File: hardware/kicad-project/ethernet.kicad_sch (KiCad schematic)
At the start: 43 parts, among them IC7 IC_ETH_PHY_LAN8742A, J2 J_RJ45_SKT_MAG_LED, Y3 25MHZ

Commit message: Added MCU decoupling
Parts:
- renumbered C45 to C30, C46 to C31, C47 to C32, C48 to C33, C49 to C34, C50 to C35, C51 to C36, C52 to C37, C53 to C38, C54 to C39, IC7 to IC6, J2 to J8, NT1 to NT3, R50 to R20, R51 to R21, R52 to R22, R56 to R23, R59 to R24, R54 to R25, R57 to R26, R58 to R27, R53 to R28, R55 to R29, R60 to R30, R61 to R31, R62 to R32, R63 to R33, R64 to R34, R47 to R35, R48 to R36, R49 to R37, TP23 to TP19, TP24 to TP20, TP25 to TP21, TP26 to TP22, TP27 to TP23, TP28 to TP24, Y3 to Y2
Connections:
- net GNDA renamed Earth

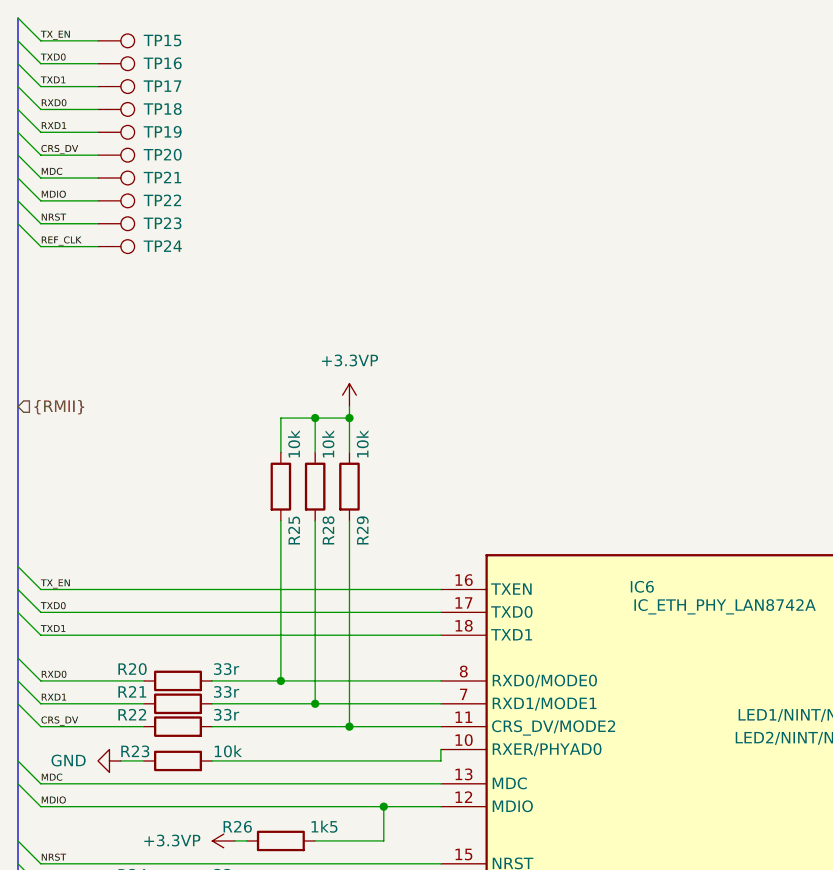
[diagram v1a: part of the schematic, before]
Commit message: Adding test points
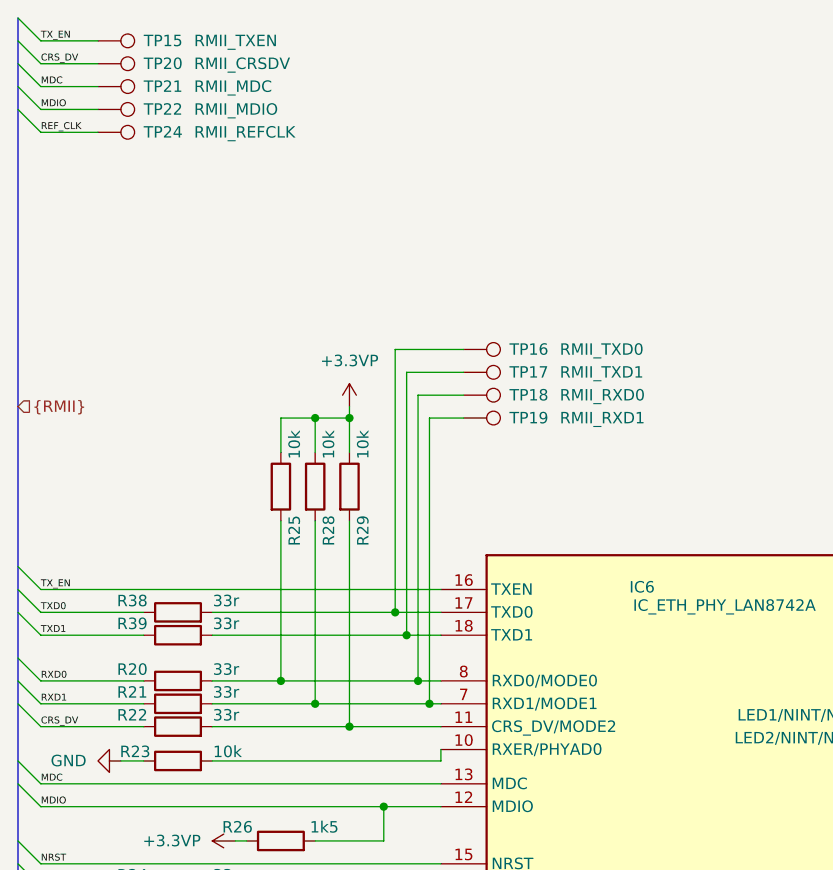
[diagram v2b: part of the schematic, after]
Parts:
- removed TP16, TP17, TP18, TP19, TP23: (no value), TestPoint:TestPoint_THTPad_D1.0mm_Drill0.5mm, symbol Connector:TestPoint
- added R38, R39: 33r, Resistor_SMD:R_0603_1608Metric_Pad0.98x0.95mm_HandSolder, symbol #InvenTree:R_33r_0603
- added TP16: RMII_TXD0, ebnx_footprints:TestPoint_THTPad_D1.0mm_Drill0.5mm_annotated, symbol ebnx_symbols:TestPoint_Annotated_Silkscreen
- added TP17: RMII_TXD1, ebnx_footprints:TestPoint_THTPad_D1.0mm_Drill0.5mm_annotated, symbol ebnx_symbols:TestPoint_Annotated_Silkscreen
- added TP18: RMII_RXD0, ebnx_footprints:TestPoint_THTPad_D1.0mm_Drill0.5mm_annotated, symbol ebnx_symbols:TestPoint_Annotated_Silkscreen
- added TP19: RMII_RXD1, ebnx_footprints:TestPoint_THTPad_D1.0mm_Drill0.5mm_annotated, symbol ebnx_symbols:TestPoint_Annotated_Silkscreen
- TP15: value (none) -> RMII_TXEN; footprint TestPoint:TestPoint_THTPad_D1.0mm_Drill0.5mm -> ebnx_footprints:TestPoint_THTPad_D1.0mm_Drill0.5mm_annotated; symbol Connector:TestPoint -> ebnx_symbols:TestPoint_Annotated_Silkscreen; now in the parts list
- TP20: value (none) -> RMII_CRSDV; footprint TestPoint:TestPoint_THTPad_D1.0mm_Drill0.5mm -> ebnx_footprints:TestPoint_THTPad_D1.0mm_Drill0.5mm_annotated; symbol Connector:TestPoint -> ebnx_symbols:TestPoint_Annotated_Silkscreen; now in the parts list
- TP21: value (none) -> RMII_MDC; footprint TestPoint:TestPoint_THTPad_D1.0mm_Drill0.5mm -> ebnx_footprints:TestPoint_THTPad_D1.0mm_Drill0.5mm_annotated; symbol Connector:TestPoint -> ebnx_symbols:TestPoint_Annotated_Silkscreen; now in the parts list
- TP22: value (none) -> RMII_MDIO; footprint TestPoint:TestPoint_THTPad_D1.0mm_Drill0.5mm -> ebnx_footprints:TestPoint_THTPad_D1.0mm_Drill0.5mm_annotated; symbol Connector:TestPoint -> ebnx_symbols:TestPoint_Annotated_Silkscreen; now in the parts list
- TP24: value (none) -> RMII_REFCLK; footprint TestPoint:TestPoint_THTPad_D1.0mm_Drill0.5mm -> ebnx_footprints:TestPoint_THTPad_D1.0mm_Drill0.5mm_annotated; symbol Connector:TestPoint -> ebnx_symbols:TestPoint_Annotated_Silkscreen; now in the parts list
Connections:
- net TXD0: now also R38.1; no longer IC6.17 (TXD0)
- net TXD1: now also R39.1; no longer IC6.18 (TXD1)
- net at IC6.8 (RXD0/MODE0), R20.2, R25.2: now also TP18.1
- net at IC6.7 (RXD1/MODE1), R21.2, R28.2: now also TP19.1
- new net: IC6.17 (TXD0), R38.2, TP16.1
- new net: IC6.18 (TXD1), R39.2, TP17.1
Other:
- moved on the sheet: TP20, TP21, TP22, TP24

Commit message: v0.5 routing complete
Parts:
- removed C38, C39: 100nF, Capacitor_SMD:C_0603_1608Metric_Pad1.08x0.95mm_HandSolder, symbol #InvenTree:C_100n_0603
